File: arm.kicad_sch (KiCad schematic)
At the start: 37 parts, among them J1 TC2030-IDC-NL, U10 24CW1280T, U4 STM32F103T6U6A, U6 KTD2052, U7 TLT9251VLE, U8 MAX17671FATB+

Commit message: Cleanup the project after moving to KiCad.
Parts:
- removed C11: 100nF, PCB-lqeomw61a722wi99q4vw-1, symbol mikona-altium-import:1_SYM-773ebe35ab3ba8f9-3
- removed C12: 10 µF, RESC2013X55X40ML15T20, symbol mikona-altium-import:1_SYM-55069f29b9a38ac1-2
- removed C13, C14, C15, C16, C19, C20: 100nF, PCB-ya5qsrmvtd5pjczft90h-1, symbol mikona-altium-import:1_SYM-f7023f833ffb28c5-1
- removed C17: 10uF, PCB-8tuutlkq7p1aj3t2dfdp-1, symbol mikona-altium-import:1_SYM-55c098f4cfa08a07-1
- removed C24: 1uF, CAPC1608X90X35ML15T15, symbol mikona-altium-import:1_SYM-ce7a065e703111bd-1
- removed C25: 2.2uF, CAPC1608X90X35LL10T15, symbol mikona-altium-import:1_CAP-2
- removed C26: 4.7uF, CAPC1608X90X35NL10T15, symbol mikona-altium-import:1_GRM188Z71C475KE21J
- removed D4: Lite-On LTST-C19HE1WT, PCB-52d9enhv62acg8agpph7-1, symbol mikona-altium-import:3_SYM-1946d08468e8c681-4
- removed FB2: 100, MURA-BLM18KG_TN-B60-CHIP-2_V3, symbol mikona-altium-import:0_MURA-FB-2
- removed J1: TC2030-IDC-NL, PCB-ltb50y2q1twco73v61fe-1, symbol mikona-altium-import:0_TC2030-MCP-NL-Symbol-1
- removed L2: 68.0µH, PCB-o31o4oqkad523pnvsppd-1, symbol mikona-altium-import:0_SYM-3019f8d9a4f8efde-1
- removed R13, R2, R27, R28, R29, R30, R4: 100K, RESC1005X40X25ML10T10, symbol mikona-altium-import:0_RES-2
- removed R17: 0, RESC1005X40X25ML05T10, symbol mikona-altium-import:0_RES-2
- removed R18: 100K, RESC1005X40X25ML10T10, symbol mikona-altium-import:2_RES-2
- removed R19: 120, RESC1005X37X25LL05T10, symbol mikona-altium-import:1_RES-2
- removed R22: 0, RESC1005X40X25ML05T10, symbol mikona-altium-import:2_RES-2
- removed R23: 787K, RESC1005X40X25LL05T05, symbol mikona-altium-import:0_RES-2
- removed R24: 3.32M, RESC1005X40X25NL05T05, symbol mikona-altium-import:1_RES-2
- removed R25, R26: 4.7K, RESC1005X40X25NL05T05, symbol mikona-altium-import:0_SYM-e02329a4a0913fe4-1
- removed U10: 24CW1280T, PCB-du7oa82jyfofml92o6ch-1, symbol mikona-altium-import:0_SYM-b1fc7d542f6b6e3b-1
- removed U4: STM32F103T6U6A, STM-VFQFPN36_L, symbol mikona-altium-import:0_MC-ARM-STM32F103X4_6-SQ37
- removed U6: KTD2052, PCB-1zdkv4te5dlcf1e3m0hc-1, symbol mikona-altium-import:0_KTD2052
- removed U7: TLT9251VLE, PCB-is4r40753zstvrjiqh7i-1, symbol mikona-altium-import:0_Infineon TLT9251VLEXUMA1-Symbol-1
- removed U8: MAX17671FATB+, T1033+1_V, symbol mikona-altium-import:0_Maxim Integrated MAX17671FATB+
- added C11, C14, C15, C16, C19, C20, C22: 100nF, Capacitor_SMD:C_0402_1005Metric_Pad0.74x0.62mm_HandSolder, symbol Device:C_Small
- added C12: 10µF, Capacitor_SMD:C_0805_2012Metric_Pad1.18x1.45mm_HandSolder, symbol Device:C_Small
- added C17: 10uF, Capacitor_SMD:C_0402_1005Metric_Pad0.74x0.62mm_HandSolder, symbol Device:C_Small
- added C24: 10uF, Capacitor_SMD:C_0603_1608Metric_Pad1.08x0.95mm_HandSolder, symbol Device:C_Small
- added C25, C29: 2.2uF, Capacitor_SMD:C_0402_1005Metric_Pad0.74x0.62mm_HandSolder, symbol Device:C_Small
- added C26, C28: 22uF, Capacitor_SMD:C_0805_2012Metric_Pad1.18x1.45mm_HandSolder, symbol Device:C_Small
- added D4: RGB, LED_SMD:LED_LiteOn_LTST-C19HE1WT, symbol Device:LED_RGBA
- added FB2: FerriteBead_Small, Resistor_SMD:R_0603_1608Metric_Pad0.98x0.95mm_HandSolder, symbol Device:FerriteBead_Small
- added J1: TC2030-IDC-NL, Connector:Tag-Connect_TC2030-IDC-NL_2x03_P1.27mm_Vertical, symbol Connector:Conn_ARM_SWD_TagConnect_TC2030-NL
- added L2: 4.7uH, Inductor_SMD:L_Taiyo-Yuden_NR-50xx_HandSoldering, symbol Device:L
- added R13, R22, R24: 0, Resistor_SMD:R_0402_1005Metric_Pad0.72x0.64mm_HandSolder, symbol Device:R_Small_US
- added R19: 120, Resistor_SMD:R_0402_1005Metric_Pad0.72x0.64mm_HandSolder, symbol Device:R_Small_US
- added R2: 100K, Resistor_SMD:R_0402_1005Metric_Pad0.72x0.64mm_HandSolder, symbol Device:R_Small_US
- added RN1, RN3: 100K, Resistor_SMD:R_Array_Convex_2x0402, symbol Device:R_Pack02
- added RN2: 4.7K, Resistor_SMD:R_Array_Convex_2x0402, symbol Device:R_Pack02
- added U10: MX25V1006FZUI, MX25V1006FZUI:MX25V1006FZUI, symbol MX25V1006FZUI:MX25V1006FZUI
- added U11: MIC5528-3.3, MIC5528-3.3YMT-TR:SON40P120X120X60-7N, symbol MIC5528-3.3YMT-TR:MIC5528-3.3YMT-TR
- added U4: STM32F042G6Ux, Package_DFN_QFN:QFN-28_4x4mm_P0.5mm, symbol MCU_ST_STM32F0:STM32F042G6Ux
- added U6: KTD2026EWE-TR, KTD2026EWE-TR:SON40P150X150X55-9N, symbol KTD2026EWE-TR:KTD2026EWE-TR
- added U7: ATA6561-GBQW, ATA6561-GBQW:SON65P300X300X100-9N, symbol ATA6561-GBQW:ATA6561-GBQW
- added U8: AP63205WU, Package_TO_SOT_SMD:TSOT-23-6, symbol Regulator_Switching:AP63205WU
- C27: footprint PCB-ya5qsrmvtd5pjczft90h-1 -> Capacitor_SMD:C_0402_1005Metric_Pad0.74x0.62mm_HandSolder; symbol mikona-altium-import:1_SYM-f7023f833ffb28c5-1 -> Device:C_Small
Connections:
- net 3V3 is gone; now on net GND: C27.2
- net CAN_N: now also R19.2, U7.6 (CANL)
- net CAN_P: now also R19.1, U7.7 (CANH)
- net CAN_RX: now also U4.19 (PA9/PA11), U7.4 (RXD)
- net CAN_STB: now also U4.15 (PB1), U7.8 (STBY)
- net CAN_TX: now also U4.20 (PA10/PA12), U7.1 (TXD)
- net CHARGE: now also RN1.1 (R1.1), U4.6 (PA0)
- net DISCHARGE: now also RN1.2 (R2.1), U4.8 (PA2)
- net DONE: now also U4.7 (PA1)
- net GND: now also C11.2, C12.1, C14.2, C15.2, C16.2, C17.2, C19.2, C20.2, C24.2, C25.2, C26.2, C28.2, C29.2, J1.5 (GND), RN1.3 (R2.2), RN1.4 (R1.2), RN3.3 (R2.2), RN3.4 (R1.2), U10.4 (GND), U10.9 (GND), U11.3 (GND), U11.7 (GND), U4.16 (VSSA), U6.8 (GND), U6.9 (EP), U7.2 (GND), U7.9 (EXP), U8.4 (GND); no longer C27.1
- net KICK_A: now also RN3.2 (R2.1), U4.11 (PA5)
- net KICK_B: now also RN3.1 (R1.1), U4.10 (PA4)
- net SCL: now also RN2.3 (R2.2), U4.3 (PF1), U6.6 (SCL)
- net SDA: now also RN2.4 (R1.2), U4.2 (PF0), U6.7 (SDA)
- net SWCLK: now also J1.4 (SWCLK), U4.22 (PA14)
- net SWDIO: now also J1.2 (SWDIO), U4.21 (PA13)
- net SW_NRST: now also J1.3 (~{RESET}), R22.2
- net VOUT_ADC: now also U4.9 (PA3)
- new net: R2.2, U6.1 (ST)
- new net: D4.3 (BK), U6.2 (D3)
- new net: D4.2 (GK), U6.3 (D2)
- new net: D4.1 (RK), U6.4 (D1)
- new net: C24.1, FB2.2, R24.2, U8.3 (IN)
- new net: C11.1, R22.1, U4.4 (NRST)
- new net: R24.1, U8.2 (EN)
- new net: C22.2, L2.1, U8.5 (SW)
- new net: C22.1, U8.6 (BST)
- new net: R13.2, U11.4 (EN)
- new net +24V: FB2.1
- new net +3.3V: C14.1, C15.1, C16.1, C17.1, C19.1, C27.1, C29.1, J1.1 (VCC), RN2.1 (R1.1), RN2.2 (R2.1), U10.8 (VCC), U11.1 (VOUT), U11.2 (VOUT), U4.17 (VDD), U4.18 (VDDIO2), U4.5 (VDDA), U7.5 (VIO)
- new net +5V: C12.2, C20.1, C25.1, C26.1, C28.1, D4.4 (A), L2.2, R13.1, R2.1, U11.6 (VIN), U6.5 (VIN), U7.3 (VCC), U8.1 (FB)
- new net FLASH_CS: U10.1 (CS#), U4.27 (PB6)
- new net FLASH_WP: U10.3 (WP#), U4.28 (PB7)
- new net MISO: U10.2 (SO/SIO1), U4.25 (PB4)
- new net MOSI: U10.5 (SI/SIO0), U4.26 (PB5)
- new net SCK: U10.6 (SCLK), U4.24 (PB3)
- no-connect marks 0 -> 6
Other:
- note added: "Flash"
- note added: "IO"
- note removed: "Misc"

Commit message: Add missing 3d models.
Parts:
- D4: footprint LED_SMD:LED_LiteOn_LTST-C19HE1WT -> LTST-C19HE1WT:LED_LiteOn_LTST-C19HE1WT
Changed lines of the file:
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@@
       (effects (font (size 1.27 1.27)))
     )
-    (property "Footprint" "LED_SMD:LED_LiteOn_LTST-C19HE1WT" (at 228.6 106.68 0)
+    (property "Footprint" "LTST-C19HE1WT:LED_LiteOn_LTST-C19HE1WT" (at 228.6 106.68 0)
       (effects (font (size 1.27 1.27)) hide)
     )

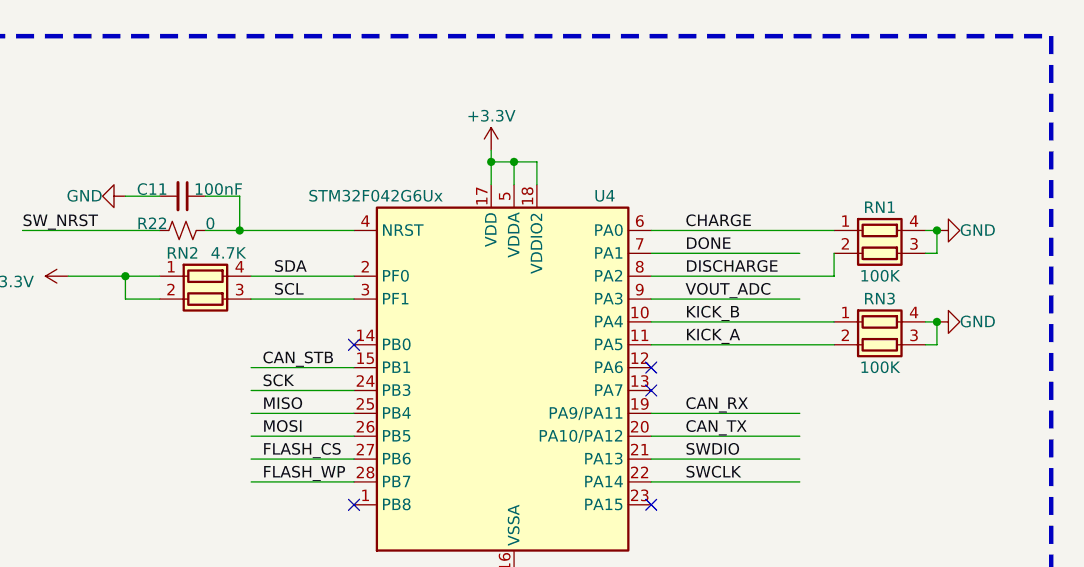
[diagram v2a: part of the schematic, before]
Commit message: Finish the layout, remove old routings, and setup internal planes.
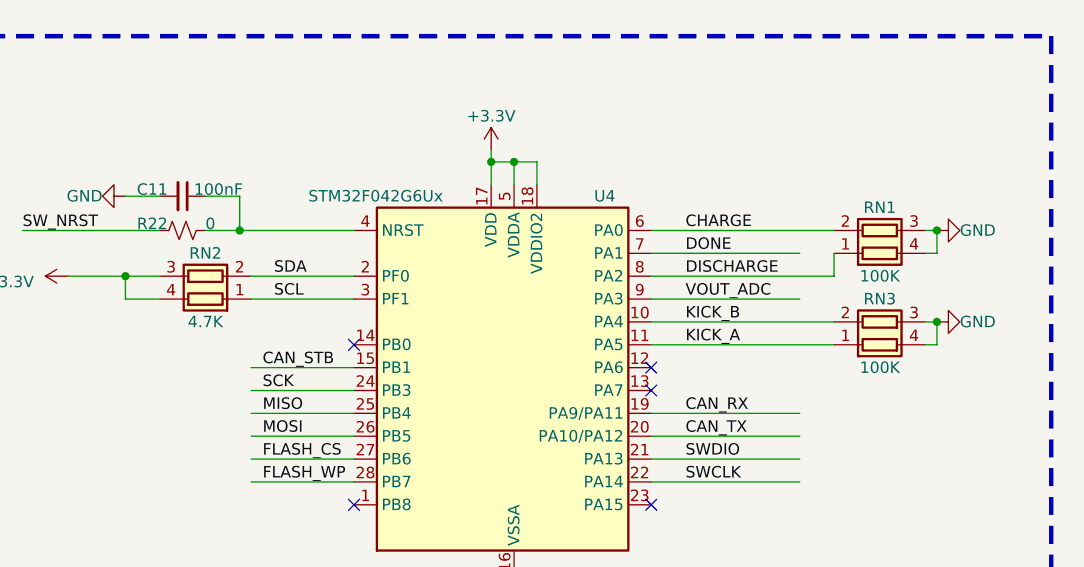
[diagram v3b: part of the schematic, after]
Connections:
- net +3.3V: now also RN2.3 (R2.2), RN2.4 (R1.2); no longer RN2.1 (R1.1), RN2.2 (R2.1)
- net CHARGE: now also RN1.2 (R2.1); no longer RN1.1 (R1.1)
- net DISCHARGE: now also RN1.1 (R1.1); no longer RN1.2 (R2.1)
- net KICK_A: now also RN3.1 (R1.1); no longer RN3.2 (R2.1)
- net KICK_B: now also RN3.2 (R2.1); no longer RN3.1 (R1.1)
- net SCL: now also RN2.1 (R1.1); no longer RN2.3 (R2.2)
- net SDA: now also RN2.2 (R2.1); no longer RN2.4 (R1.2)
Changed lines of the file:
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@@
     )
   )
-  (symbol (lib_id "power:+3.3V") (at 44.45 49.53 0) (unit 1)
-    (in_bom yes) (on_board yes) (dnp no)
-    (property "Reference" "#PWR01" (at 44.45 53.34 0)
-      (effects (font (size 1.27 1.27)) hide)
-    )
-    (property "Value" "+3.3V" (at 44.45 45.72 0)
-      (effects (font (size 1.27 1.27)))
-    )
-    (property "Footprint" "" (at 44.45 49.53 0)
-      (effects (font (size 1.27 1.27)) hide)
-    )
-    (property "Datasheet" "" (at 44.45 49.53 0)
-      (effects (font (size 1.27 1.27)) hide)
-    )
-    (pin "1")
-    (instances
-      (project "mikona"
-        (path "/0832a6ea-8574-47f1-9003-2905bad71af2/5ee3a2c7-8940-4f63-baa3-da8fb21e9af5"
-          (reference "#PWR01") (unit 1)
-        )
-      )
-    )
-  )
-  (symbol (lib_id "Device:LED_RGBA") (at 228.6 107.95 180) (unit 1)
-    (in_bom yes) (on_board yes) (dnp no)
-    (property "Reference" "D4" (at 226.06 99.06 0)
-      (effects (font (size 1.27 1.27)))
-    )
-    (property "Value" "RGB" (at 231.14 99.06 0)
-      (effects (font (size 1.27 1.27)))
-    )
-    (property "Footprint" "LTST-C19HE1WT:LED_LiteOn_LTST-C19HE1WT" (at 228.6 106.68 0)
-      (effects (font (size 1.27 1.27)) hide)
-    )
-    (property "Datasheet" "~" (at 228.6 106.68 0)
-      (effects (font (size 1.27 1.27)) hide)
-    )
-    (property "Part" "LTST-C19HE1WT" (at 228.6 107.95 0)
+  (symbol (lib_id "Device:R_Pack02") (at 97.79 31.75 90) (unit 1)
+    (in_bom yes) (on_board yes) (dnp no)
+    (property "Reference" "RN2" (at 97.79 29.21 90)
+      (effects (font (size 1.27 1.27)))
+    )
+    (property "Value" "4.7K" (at 97.79 36.83 90)
+      (effects (font (size 1.27 1.27)))
+    )
+    (property "Footprint" "Resistor_SMD:R_Array_Convex_2x0402" (at 97.79 27.305 90)
+      (effects (font (size 1.27 1.27)) hide)
+    )
+    (property "Datasheet" "~" (at 97.79 31.75 0)
+      (effects (font (size 1.27 1.27)) hide)
+    )
+    (property "Part" "EXB-24V472JX" (at 97.79 31.75 90)
       (effects (font (size 1.27 1.27)) hide)
     )
@@
       (project "mikona"
         (path "/0832a6ea-8574-47f1-9003-2905bad71af2/5ee3a2c7-8940-4f63-baa3-da8fb21e9af5"
-          (reference "D4") (unit 1)
-        )
-      )
-    )
-  )
-  (symbol (lib_id "Device:R_Pack02") (at 97.79 34.29 270) (unit 1)
-    (in_bom yes) (on_board yes) (dnp no)
-    (property "Reference" "RN2" (at 95.25 29.21 90)
-      (effects (font (size 1.27 1.27)))
-    )
-    (property "Value" "4.7K" (at 100.33 29.21 90)
-      (effects (font (size 1.27 1.27)))
-    )
-    (property "Footprint" "Resistor_SMD:R_Array_Convex_2x0402" (at 97.79 38.735 90)
-      (effects (font (size 1.27 1.27)) hide)
-    )
-    (property "Datasheet" "~" (at 97.79 34.29 0)
-      (effects (font (size 1.27 1.27)) hide)
-    )
-    (property "Part" "EXB-24V472JX" (at 97.79 34.29 90)
+          (reference "RN2") (unit 1)
+        )
+      )
+    )
+  )
+  (symbol (lib_id "power:+3.3V") (at 44.45 49.53 0) (unit 1)
+    (in_bom yes) (on_board yes) (dnp no)
+    (property "Reference" "#PWR01" (at 44.45 53.34 0)
+      (effects (font (size 1.27 1.27)) hide)
+    )
+    (property "Value" "+3.3V" (at 44.45 45.72 0)
+      (effects (font (size 1.27 1.27)))
+    )
+    (property "Footprint" "" (at 44.45 49.53 0)
+      (effects (font (size 1.27 1.27)) hide)
+    )
+    (property "Datasheet" "" (at 44.45 49.53 0)
+      (effects (font (size 1.27 1.27)) hide)
+    )
+    (pin "1")
+    (instances
+      (project "mikona"
+        (path "/0832a6ea-8574-47f1-9003-2905bad71af2/5ee3a2c7-8940-4f63-baa3-da8fb21e9af5"
+          (reference "#PWR01") (unit 1)
+        )
+      )
+    )
+  )
+  (symbol (lib_id "Device:LED_RGBA") (at 228.6 107.95 180) (unit 1)
+    (in_bom yes) (on_board yes) (dnp no)
+    (property "Reference" "D4" (at 226.06 99.06 0)
+      (effects (font (size 1.27 1.27)))
+    )
+    (property "Value" "RGB" (at 231.14 99.06 0)
+      (effects (font (size 1.27 1.27)))
+    )
+    (property "Footprint" "LTST-C19HE1WT:LED_LiteOn_LTST-C19HE1WT" (at 228.6 106.68 0)
+      (effects (font (size 1.27 1.27)) hide)
+    )
+    (property "Datasheet" "~" (at 228.6 106.68 0)
+      (effects (font (size 1.27 1.27)) hide)
+    )
+    (property "Part" "LTST-C19HE1WT" (at 228.6 107.95 0)
       (effects (font (size 1.27 1.27)) hide)
     )
@@
       (project "mikona"
         (path "/0832a6ea-8574-47f1-9003-2905bad71af2/5ee3a2c7-8940-4f63-baa3-da8fb21e9af5"
-          (reference "RN2") (unit 1)
+          (reference "D4") (unit 1)
         )
       )
@@
     )
   )
-  (symbol (lib_id "Device:R_Pack02") (at 172.72 39.37 270) (unit 1)
+  (symbol (lib_id "Device:R_Pack02") (at 172.72 36.83 270) (mirror x) (unit 1)
     (in_bom yes) (on_board yes) (dnp no)
     (property "Reference" "RN3" (at 172.72 34.29 90)
@@
       (effects (font (size 1.27 1.27)))
     )
-    (property "Footprint" "Resistor_SMD:R_Array_Convex_2x0402" (at 172.72 43.815 90)
-      (effects (font (size 1.27 1.27)) hide)
-    )
-    (property "Datasheet" "~" (at 172.72 39.37 0)
-      (effects (font (size 1.27 1.27)) hide)
-    )
-    (property "Part" "EXB-24V104JX" (at 172.72 39.37 90)
+    (property "Footprint" "Resistor_SMD:R_Array_Convex_2x0402" (at 172.72 32.385 90)
+      (effects (font (size 1.27 1.27)) hide)
+    )
+    (property "Datasheet" "~" (at 172.72 36.83 0)
+      (effects (font (size 1.27 1.27)) hide)
+    )
+    (property "Part" "EXB-24V104JX" (at 172.72 36.83 90)
       (effects (font (size 1.27 1.27)) hide)
     )
@@
     )
   )
-  (symbol (lib_id "Device:R_Pack02") (at 172.72 29.21 270) (unit 1)
+  (symbol (lib_id "Device:R_Pack02") (at 172.72 26.67 270) (mirror x) (unit 1)
     (in_bom yes) (on_board yes) (dnp no)
     (property "Reference" "RN1" (at 172.72 24.13 90)
@@
       (effects (font (size 1.27 1.27)))
     )
-    (property "Footprint" "Resistor_SMD:R_Array_Convex_2x0402" (at 172.72 33.655 90)
-      (effects (font (size 1.27 1.27)) hide)
-    )
-    (property "Datasheet" "~" (at 172.72 29.21 0)
-      (effects (font (size 1.27 1.27)) hide)
-    )
-    (property "Part" "EXB-24V104JX" (at 172.72 29.21 90)
-      (effects (font (size 1.27 1.27)) hide)
-    )
+    (property "Footprint" "Resistor_SMD:R_Array_Convex_2x0402" (at 172.72 22.225 90)
+      (effects (font (size 1.27 1.27)) hide)
+    )
+    (property "Datasheet" "~" (at 172.72 26.67 0)
+      (effects (font (size 1.27 1.27)) hide)
+    )
+    (property "Part" "EXB-24V104JX" (at 172.72 26.67 90)
+      (effects (font (size 1.27 1.27)) hide)
+    )

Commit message: Finish the draft routing.
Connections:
- net +3.3V: now also RN2.1 (R1.1), RN2.2 (R2.1); no longer RN2.3 (R2.2), RN2.4 (R1.2)
- net SCL: now also RN2.4 (R1.2); no longer RN2.1 (R1.1)
- net SDA: now also RN2.3 (R2.2); no longer RN2.2 (R2.1)
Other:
- moved on the sheet: RN2
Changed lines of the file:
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@@
     )
   )
-  (symbol (lib_id "Device:R_Pack02") (at 97.79 31.75 90) (unit 1)
+  (symbol (lib_id "Device:R_Pack02") (at 97.79 31.75 270) (mirror x) (unit 1)
     (in_bom yes) (on_board yes) (dnp no)
     (property "Reference" "RN2" (at 97.79 29.21 90)

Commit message: Add jlpcb rules and fix many violations.
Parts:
- U10: footprint MX25V1006FZUI:MX25V1006FZUI -> MX25V1006FZUI:PSON50P200X300X60-9N
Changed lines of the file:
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@@
       (effects (font (size 1.524 1.524)))
     )
-    (property "Footprint" "MX25V1006FZUI:MX25V1006FZUI" (at 177.8 95.504 0)
+    (property "Footprint" "MX25V1006FZUI:PSON50P200X300X60-9N" (at 177.8 95.504 0)
       (effects (font (size 1.524 1.524)) hide)
     )

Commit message: Improve regulator routing.
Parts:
- C25, C29: Part (none) -> LMK105ABJ225KVHF
- U7: value ATA6561-GBQW -> ATA6561-GBQW-N
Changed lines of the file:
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@@
+      (effects (font (size 1.27 1.27)) hide)
+    )
+    (property "Part" "LMK105ABJ225KVHF" (at 90.17 121.92 0)
       (effects (font (size 1.27 1.27)) hide)
     )
@@
       (effects (font (size 1.27 1.27)))
     )
-    (property "Value" "ATA6561-GBQW" (at 241.3 13.97 0)
+    (property "Value" "ATA6561-GBQW-N" (at 240.03 13.97 0)
       (effects (font (size 1.27 1.27)))
     )
@@
       (effects (font (size 1.27 1.27)) hide)
     )
+    (property "Part" "LMK105ABJ225KVHF" (at 34.29 121.92 0)
+      (effects (font (size 1.27 1.27)) hide)
+    )
